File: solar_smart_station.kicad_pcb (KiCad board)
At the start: 6 copper layers, 46 parts, among them J1 CE, J2 CE, J3 Conn_01x03_Pin, J4 JST_VH_B2P_3.96mm, J5 JST_VH_B2P_3.96mm, J6 JST_VH_B3P_3.96mm, U1 BQ25672RQMR, U2 TLV73333PDBV, U3 MSPM0C1104SDSGR

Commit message: First layout
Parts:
- removed J6: JST_VH_B3P_3.96mm, Connector_JST:JST_VH_B3P-VH_1x03_P3.96mm_Vertical
- removed TP2: Thermistor, Connector_PinHeader_2.54mm:PinHeader_1x01_P2.54mm_Vertical
- added C23: 0.1uF, Capacitor_SMD:C_0603_1608Metric, F.Cu at (78.0, 174.5)
- added C24: 0.1uF, Capacitor_SMD:C_0603_1608Metric, F.Cu at (78.0, 171.5)
- added C25: 0.1uF, Capacitor_SMD:C_0603_1608Metric, F.Cu at (78.0, 168.5)
- added C26: 0.1uF, Capacitor_SMD:C_0603_1608Metric, F.Cu at (78.0, 165.5)
- added C27: 0.1uF, Capacitor_SMD:C_0603_1608Metric, F.Cu at (78.0, 162.5)
- added C28: 0.1uF, Capacitor_SMD:C_0603_1608Metric, F.Cu at (78.0, 159.5)
- added C29: 1uF, Capacitor_SMD:C_0603_1608Metric, F.Cu at (72.5, 170.0)
- added C30: 1uF, Capacitor_SMD:C_0603_1608Metric, F.Cu at (68.5, 170.0)
- added C31: 0.1uF, Capacitor_SMD:C_0603_1608Metric, F.Cu at (78.0, 157.0)
- added C32: 0.1uF, Capacitor_SMD:C_0603_1608Metric, F.Cu at (76.5, 155.0)
- added C33: 0.1uF, Capacitor_SMD:C_0603_1608Metric, F.Cu at (79.5, 155.0)
- added D1: LED, LED_SMD:LED_0603_1608Metric, F.Cu at (35.5, 162.0)
- added D2: Schottky_30V_1A, solar_station:DIO_RB02_ROM, F.Cu at (71.5, 157.0)
- added H1: MountingHole_Pad, TestPoint:TestPoint_THTPad_2.5x2.5mm_Drill1.2mm, F.Cu at (84.0, 175.5)
- added H2: MountingHole_Pad, TestPoint:TestPoint_THTPad_2.5x2.5mm_Drill1.2mm, F.Cu at (84.0, 171.5)
- added H3: MountingHole_Pad, TestPoint:TestPoint_THTPad_2.5x2.5mm_Drill1.2mm, F.Cu at (84.0, 167.5)
- added H4: MountingHole_Pad, TestPoint:TestPoint_THTPad_2.5x2.5mm_Drill1.2mm, F.Cu at (84.0, 163.5)
- added H5: MountingHole_Pad, TestPoint:TestPoint_THTPad_2.5x2.5mm_Drill1.2mm, F.Cu at (84.0, 159.5)
- added H6: MountingHole_Pad, TestPoint:TestPoint_THTPad_2.5x2.5mm_Drill1.2mm, F.Cu at (84.0, 155.5)
- added H7: MountingHole_Pad, MountingHole:MountingHole_3.2mm_M3_DIN965_Pad_TopBottom, F.Cu at (34.2, 150.2)
- added H8: MountingHole_Pad, MountingHole:MountingHole_3.2mm_M3_DIN965_Pad_TopBottom, F.Cu at (83.2, 150.0)
- added H9: MountingHole_Pad, MountingHole:MountingHole_3.2mm_M3_DIN965_Pad_TopBottom, F.Cu at (83.2, 181.2)
- added J7: Thermistor_1, Connector_PinHeader_2.54mm:PinHeader_1x02_P2.54mm_Vertical, F.Cu at (51.2, 181.0)
- added J8: Thermistor_2, Connector_PinHeader_2.54mm:PinHeader_1x02_P2.54mm_Vertical, F.Cu at (58.2, 181.0)
- added NT1: NetTie_3, NetTie:NetTie-3_SMD_Pad0.5mm, F.Cu at (47.5, 170.5)
- added NT2: NetTie_2, NetTie:NetTie-2_SMD_Pad0.5mm, F.Cu at (74.5, 179.0)
- added Q1: AO3400A, Package_TO_SOT_SMD:SOT-23, F.Cu at (72.4, 152.0)
- added Q2: AO3400A, Package_TO_SOT_SMD:SOT-23, F.Cu at (68.4, 152.0)
- added R13: 1kR, Resistor_SMD:R_0402_1005Metric, F.Cu at (79.5, 174.5)
- added R14: 1kR, Resistor_SMD:R_0402_1005Metric, F.Cu at (79.5, 171.5)
- added R15: 1kR, Resistor_SMD:R_0402_1005Metric, F.Cu at (79.5, 168.5)
- added R16: 1kR, Resistor_SMD:R_0402_1005Metric, F.Cu at (79.5, 165.5)
- added R17: 1kR, Resistor_SMD:R_0402_1005Metric, F.Cu at (79.5, 162.5)
- added R18: 1kR, Resistor_SMD:R_0402_1005Metric, F.Cu at (79.5, 159.5)
- added R19: 1kR, Resistor_SMD:R_0402_1005Metric, F.Cu at (78.5, 177.0)
- added R20: 100R, Resistor_SMD:R_0402_1005Metric, F.Cu at (79.0, 153.0)
- added R21: 10mR, Resistor_SMD:R_0805_2012Metric, F.Cu at (78.0, 151.0)
- added R22: 100R, Resistor_SMD:R_0402_1005Metric, F.Cu at (77.0, 153.0)
- added R23: 4.7kR, Resistor_SMD:R_0402_1005Metric, F.Cu at (73.5, 157.5)
- added R24: 1MegR, Resistor_SMD:R_0402_1005Metric, F.Cu at (75.0, 152.0)
- added R25: 1MegR, Resistor_SMD:R_0402_1005Metric, F.Cu at (69.5, 156.3)
- added R26: 3.3MegR, Resistor_SMD:R_0402_1005Metric, F.Cu at (65.5, 152.0)
- added R27: 10kR, Resistor_SMD:R_0402_1005Metric, F.Cu at (65.0, 167.0)
- added R28: 100kR, Resistor_SMD:R_0402_1005Metric, F.Cu at (65.0, 163.0)
- added R29: 450kR, Resistor_SMD:R_0402_1005Metric, F.Cu at (65.0, 161.0)
- added R30: 10kR, Resistor_SMD:R_0402_1005Metric, F.Cu at (65.0, 165.0)
- added U4: BQ7791500PWR, solar_station:PW24_TEX, F.Cu at (70.5, 164.5)
- added U5: CSD25402Q3A, Package_SON:VSON-8_3.3x3.3mm_P0.65mm_NexFET, F.Cu at (66.5, 157.0)
- C10, C2, C9: footprint Capacitor_SMD:C_0603_1608Metric -> Capacitor_SMD:C_0402_1005Metric
- J2: value CE -> LDO_EN
- J3: value Conn_01x03_Pin -> Conn_01x05_Pin; footprint Connector_PinSocket_2.54mm:PinSocket_1x03_P2.54mm_Vertical -> Connector_PinHeader_2.54mm:PinHeader_1x05_P2.54mm_Vertical
- U3: footprint Package_TO_SOT_SMD:TSOT-23-8 -> solar_station:TSOT-23-8-shrink
- moved J4 51.7 mm to (32.7, 179.9)
- moved C18 33.6 mm to (58.0, 158.5), turned to -90 degrees
- moved J3 32.5 mm to (75.1, 181.0), turned to -90 degrees
- moved C21 31.8 mm to (44.5, 170.5), turned to 180 degrees
- moved C22 31.2 mm to (44.5, 172.0), turned to 180 degrees
- moved R12 29.5 mm to (43.5, 175.5), turned to 90 degrees
- moved R9 28.8 mm to (47.0, 172.0), turned to 180 degrees
- moved J5 28.3 mm to (61.3, 151.3), turned to 180 degrees
- moved R11 28.3 mm to (48.5, 176.5), turned to 90 degrees
- moved R10 28.3 mm to (48.5, 174.5), turned to -90 degrees
- moved C16 27.5 mm to (55.5, 158.5), turned to -90 degrees
- moved C14 26.7 mm to (59.2, 163.5), turned to 90 degrees
- moved U3 26.3 mm to (46.0, 175.5), turned to -90 degrees
- moved C11 24.7 mm to (56.8, 163.5), turned to 90 degrees
- moved L1 22.7 mm to (48.5, 152.0)
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- renumbered C22 to C20, C20 to C21, C21 to C22
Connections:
- net +12V renamed +21V
- net Net-(J1-Pin_1) renamed CE_N
- net Net-(J2-Pin_2) renamed LDO_IN
- net Net-(J3-Pin_2) renamed SWDIO
- net Net-(J3-Pin_3) renamed SWCLK
- J3 pad 1: /Project Architecture/MCU/SCL -> VCC
- R10 pad 2: /Project Architecture/MCU/INT_N -> INT_N
- R12 pad 1: /Project Architecture/MCU/SDA -> SDA
- R9 pad 2: /Project Architecture/MCU/SCL -> /Project Architecture/MCU/SCL/RST
- U1 pad 14: /Project Architecture/SolarCharger/SCL -> SCL
- U1 pad 15: /Project Architecture/SolarCharger/SDA -> SDA
- U1 pad 21: /Project Architecture/SolarCharger/INT_N -> INT_N
- U3 pad 1: /Project Architecture/MCU/INT_N -> INT_N
- U3 pad 2: /Project Architecture/MCU/SCL -> /Project Architecture/MCU/SCL/RST
- U3 pad 5: /Project Architecture/MCU/SDA -> SDA
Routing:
- net +3V3: track 0.00 -> 51.2 mm, vias 0 -> 4
- net GND: track 0.00 -> 37.4 mm, vias 0 -> 16
- net REGN: track 0.00 -> 34.1 mm, vias 0 -> 3
- net +21V: track 0.00 -> 32.3 mm
- net SWDIO: track 0.00 -> 31.0 mm, vias 0 -> 1
- net SWCLK: track 0.00 -> 27.3 mm, vias 0 -> 1
- net BATTERY_PACK: track 0.00 -> 26.1 mm, vias 0 -> 13
- net RST: track 0.00 -> 23.3 mm, vias 0 -> 1
- net THERMISTOR_2: track 0.00 -> 22.2 mm
- net Net-(U4-VDD): track 0.00 -> 21.9 mm
- net SYSTEM_LOAD: track 0.00 -> 21.6 mm
- net CE_N: track 0.00 -> 18.5 mm, vias 0 -> 1
- net THERMISTOR: track 0.00 -> 18.3 mm
- net INT_N: track 0.00 -> 17.2 mm, vias 0 -> 2
- net Net-(U1-SW2): track 0.00 -> 16.7 mm, vias 0 -> 7
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- added copper zone on F.Cu, net -BATT
- added copper zone on In1.Cu, net -BATT
- added copper zone on B.Cu, net BATTERY_PACK
- added copper zone on F.Cu, net BATTERY_PACK
- added copper zone on F.Cu, net GND
- added copper zone on In1.Cu, net GND
- added copper zone on F.Cu, net Net-(U1-SW1)
- added copper zone on F.Cu, net Net-(U1-SW2)
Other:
- board outline added: 57.8 x 39.5 mm
- copper layers 6 -> 4

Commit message: Finish layout
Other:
- board text added: "BAT+"
- board text added: "BAT-"
- board text added: "CE"
- board text added: "GND"
- board text added: "IN+"
- board text added: "LOAD"
- board text added: "Max 21V"
- board text added: "RST"
- board text added: "SWCLK"
- board text added: "SWD PRG"
- board text added: "SWDIO"
- board text added: "Ther1"
- board text added: "Ther2"
- board text added: "VC1"
- board text added: "VC2"
- board text added: "VC3"
- board text added: "VC4"
- board text added: "VCC"
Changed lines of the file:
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@@
 	)
 	(property "ASSEMBLY_NOTES" "")
-	(property "BOARD_NAME" "Board Name")
-	(property "COMPANY" "Company Name")
-	(property "DESIGNER" "Author")
+	(property "BOARD_NAME" "Balanced Solar Charger")
+	(property "COMPANY" "Electronic-Handyman")
+	(property "DESIGNER" "Nhan Duy Truong")
 	(property "FABRICATION_NOTES" "")
 	(property "GIT_HASH_PCB" "23fc206")
 	(property "GIT_HASH_SCH" "8e341b7")
-	(property "GIT_URL" "https://github.com/nguyen-v/KDT_Hierarchical_KiBot")
-	(property "PROJECT_NAME" "KiBot Project")
+	(property "GIT_URL" "https://github.com/truongduynhan/solar_smart_station.git")
+	(property "PROJECT_NAME" "LiPo Battery Charger with CI/CD using KiBot")
 	(property "RELEASE_BODY_1.0.0" "")
 	(property "RELEASE_BODY_1.0.1" "")
@@
 		(tags "Through hole pin header THT 1x05 2.54mm single row")
 		(property "Reference" "J3"
-			(at -2.5 6.33 180)
+			(at 0 -2.67 180)
 			(layer "F.SilkS")
 			(effects
@@
 		)
 		(embedded_fonts no)
-		(model "${KICAD9_3DMODEL_DIR}/Inductor_SMD.3dshapes/L_Bourns_SRP7028A_7.3x6.6mm.step"
+		(model "${KIPRJMOD}/libraries/3D/IHLP2525CZ.step"
 			(offset
-				(xyz 0 0 0)
+				(xyz -1.5 5.325 -2.4)
 			)
 			(scale
@@
 			)
 			(rotate
-				(xyz 0 0 0)
+				(xyz -90 -0 -0)
 			)
 		)
@@
 		(tags "RSX101VYM30FHTR ")
 		(property "Reference" "D2"
-			(at -2.677507 -0.09567 0)
+			(at -2 -1.75 0)
 			(unlocked yes)
 			(layer "F.SilkS")
@@
 		(layer "User.9")
 	)
+	(gr_text "SWDIO"
+		(at 73.25 179.25 90)
+		(layer "F.SilkS")
+		(effects
+			(font
+				(size 1.2 1.2)
+				(thickness 0.15)
+			)
+			(justify left bottom)
+		)
+	)
+	(gr_text "SWD PRG"
+		(at 64.75 184.75 0)
+		(layer "F.SilkS")
+		(effects
+			(font
+				(size 1.6 1.6)
+				(thickness 0.15)
+			)
+			(justify left bottom)
+		)
+	)
+	(gr_text "Ther1"
+		(at 49.5 184.75 0)
+		(layer "F.SilkS")
+		(effects
+			(font
+				(size 1.6 1.6)
+				(thickness 0.15)
+			)
+			(justify left bottom)
+		)
+	)
+	(gr_text "VCC"
+		(at 76 179 90)
+		(layer "F.SilkS")
+		(effects
+			(font
+				(size 1.2 1.2)
+				(thickness 0.15)
+			)
+			(justify left bottom)
+		)
+	)
+	(gr_text "RST"
+		(at 68.25 179.25 90)
+		(layer "F.SilkS")
+		(effects
+			(font
+				(size 1.2 1.2)
+				(thickness 0.15)
+			)
+			(justify left bottom)
+		)
+	)
+	(gr_text "GND"
+		(at 65.75 179.25 90)
+		(layer "F.SilkS")
+		(effects
+			(font
+				(size 1.2 1.2)
+				(thickness 0.15)
+			)
+			(justify left bottom)
+		)
+	)
+	(gr_text "Ther2"
+		(at 56.25 184.75 0)
+		(layer "F.SilkS")
+		(effects
+			(font
+				(size 1.6 1.6)
+				(thickness 0.15)
+			)
+			(justify left bottom)
+		)
+	)
+	(gr_text "SWCLK"
+		(at 70.75 179.25 90)
+		(layer "F.SilkS")
+		(effects
+			(font
+				(size 1.2 1.2)
+				(thickness 0.15)
+			)
+			(justify left bottom)
+		)
+	)
+	(gr_text "CE"
+		(at 44 184.75 0)
+		(layer "F.SilkS")
+		(effects
+			(font
+				(size 1.6 1.6)
+				(thickness 0.15)
+			)
+			(justify left bottom)
+		)
+	)
+	(gr_text "BAT+"
+		(at 81.5 177 0)
+		(layer "B.SilkS")
+		(effects
+			(font
+				(size 2.5 2.5)
+				(thickness 0.5)
+				(bold yes)
+			)
+			(justify left bottom mirror)
+		)
+	)
+	(gr_text "VC4"
+		(at 81.5 173 0)
+		(layer "B.SilkS")
+		(effects
+			(font
+				(size 2.5 2.5)
+				(thickness 0.5)
+				(bold yes)
+			)
+			(justify left bottom mirror)
+		)
+	)
+	(gr_text "Max 21V"
+		(at 35 177.75 270)
+		(layer "B.SilkS")
+		(effects
+			(font
+				(size 2 2)
+				(thickness 0.3125)
+			)
+			(justify left bottom mirror)
+		)
+	)
+	(gr_text "LOAD"
+		(at 62.75 153.25 90)
+		(layer "B.SilkS")
+		(effects
+			(font
+				(size 2.5 2.5)
+				(thickness 0.5)
+				(bold yes)
+			)
+			(justify left bottom mirror)
+		)
+	)
+	(gr_text "IN+"
+		(at 31 178 270)
+		(layer "B.SilkS")
+		(effects
+			(font
+				(size 2.5 2.5)
+				(thickness 0.5)
+				(bold yes)
+			)
+			(justify left bottom mirror)
+		)
+	)
+	(gr_text "VC3"
+		(at 81.5 169 0)
+		(layer "B.SilkS")
+		(effects
+			(font
+				(size 2.5 2.5)
+				(thickness 0.5)
+				(bold yes)
+			)
+			(justify left bottom mirror)
+		)
+	)
+	(gr_text "VC2"
+		(at 81.5 164.75 0)
+		(layer "B.SilkS")
+		(effects
+			(font
+				(size 2.5 2.5)
+				(thickness 0.5)
+				(bold yes)
+			)
+			(justify left bottom mirror)
+		)
+	)
+	(gr_text "VC1"
+		(at 81.5 161 0)
+		(layer "B.SilkS")
+		(effects
+			(font
+				(size 2.5 2.5)
+				(thickness 0.5)
+				(bold yes)
+			)
+			(justify left bottom mirror)
+		)
+	)
+	(gr_text "BAT-"
+		(at 81.5 156.75 0)
+		(layer "B.SilkS")
+		(effects
+			(font
+				(size 2.5 2.5)
+				(thickness 0.5)
+				(bold yes)
+			)
+			(justify left bottom mirror)
+		)
+	)
 	(gr_text "Top View"
 		(at 83.5 40 0)
@@
 	)
 	(zone
-		(net 2)
-		(net_name "GND")
+		(net 30)
+		(net_name "-BATT")
 		(layer "In1.Cu")
-		(name "L1_GND")
 		(hatch edge 0.5)
-		(connect_pads thru_hole_only
-			(clearance 0.2)
+		(priority 2)
+		(connect_pads yes
+			(clearance 0)
 		)
 		(min_thickness 0.25)
@@
 		(polygon
 			(pts
-				(xy 30.75 146.75) (xy 70 146.5) (xy 70 184.75) (xy 30.75 185)
+				(xy 70 146.5) (xy 86.75 146.5) (xy 86.75 184.75) (xy 64 184.75) (xy 64 154.75) (xy 70 154.75)
 			)
 		)
 	)
 	(zone
-		(net 30)
-		(net_name "-BATT")
+		(net 2)
+		(net_name "GND")
 		(layer "In1.Cu")
+		(name "L1_GND")
 		(hatch edge 0.5)
-		(priority 2)
-		(connect_pads yes
-			(clearance 0)
+		(connect_pads thru_hole_only
+			(clearance 0.2)
 		)
 		(min_thickness 0.25)
@@
 		(polygon
 			(pts
-				(xy 70 146.5) (xy 86.75 146.5) (xy 86.75 184.75) (xy 64 184.75) (xy 64 154.75) (xy 70 154.75)
+				(xy 30.75 146.75) (xy 70 146.5) (xy 70 184.75) (xy 30.75 185)
 			)
 		)

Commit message: Fix ERC
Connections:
- net REGN renamed REGN_5V
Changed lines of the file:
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@@
 	(net 19 "Net-(D1-K)")
 	(net 20 "+21V")
-	(net 21 "REGN")
+	(net 21 "REGN_5V")
 	(net 22 "Net-(U3-PA24{slash}A3)")
 	(net 23 "/Project Architecture/SolarCharger/QON")
@@
 			(layers "F.Cu" "F.Mask" "F.Paste")
 			(roundrect_rratio 0.25)
-			(net 21 "REGN")
+			(net 21 "REGN_5V")
 			(pintype "passive")
 		)
@@
 			(layers "*.Cu" "*.Mask")
 			(remove_unused_layers no)
-			(net 21 "REGN")
+			(net 21 "REGN_5V")
 			(pinfunction "Pin_1")
 			(pintype "passive")
@@
 			(layers "F.Cu" "F.Mask" "F.Paste")
 			(roundrect_rratio 0.25)
-			(net 21 "REGN")
+			(net 21 "REGN_5V")
 			(pintype "passive")
 		)
@@
 			(layers "F.Cu" "F.Mask" "F.Paste")
 			(roundrect_rratio 0.25)
-			(net 21 "REGN")
+			(net 21 "REGN_5V")
 			(pintype "passive")
 		)
@@
 			(layers "F.Cu" "F.Mask" "F.Paste")
 			(roundrect_rratio 0.25)
-			(net 21 "REGN")
+			(net 21 "REGN_5V")
 			(pintype "passive")
 		)
@@
 			(size 0.599999 0.2)
 			(layers "F.Cu" "F.Mask" "F.Paste")
-			(net 21 "REGN")
+			(net 21 "REGN_5V")
 			(pinfunction "REGN")
 			(pintype "unspecified")

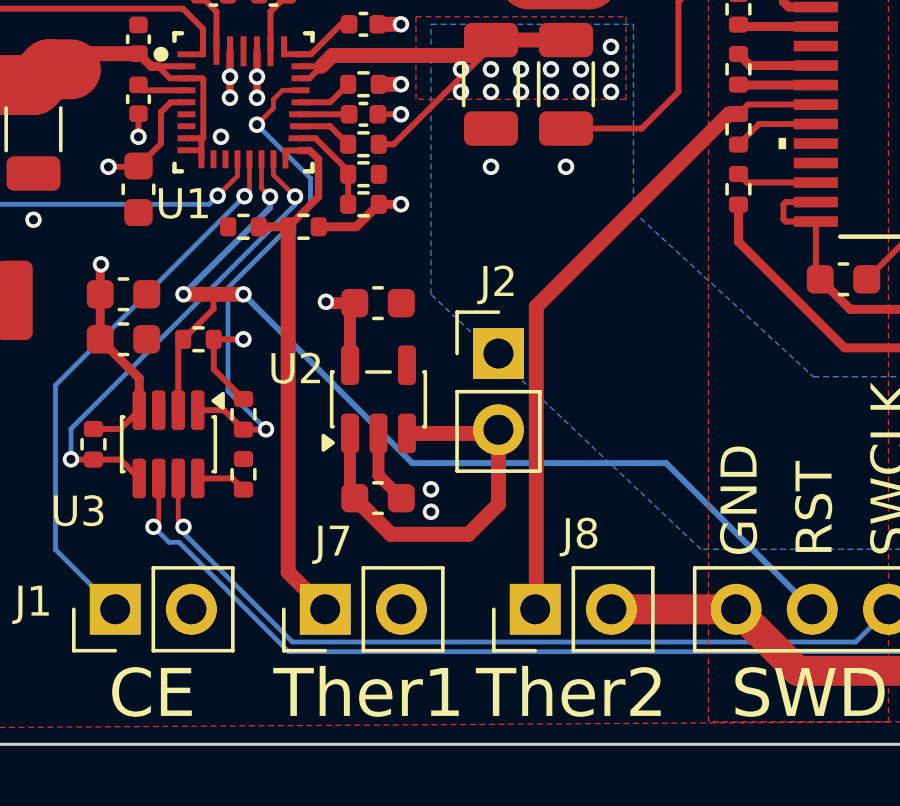
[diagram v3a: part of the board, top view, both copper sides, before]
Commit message: All connectors are deemed the same in BOM. Re-push.
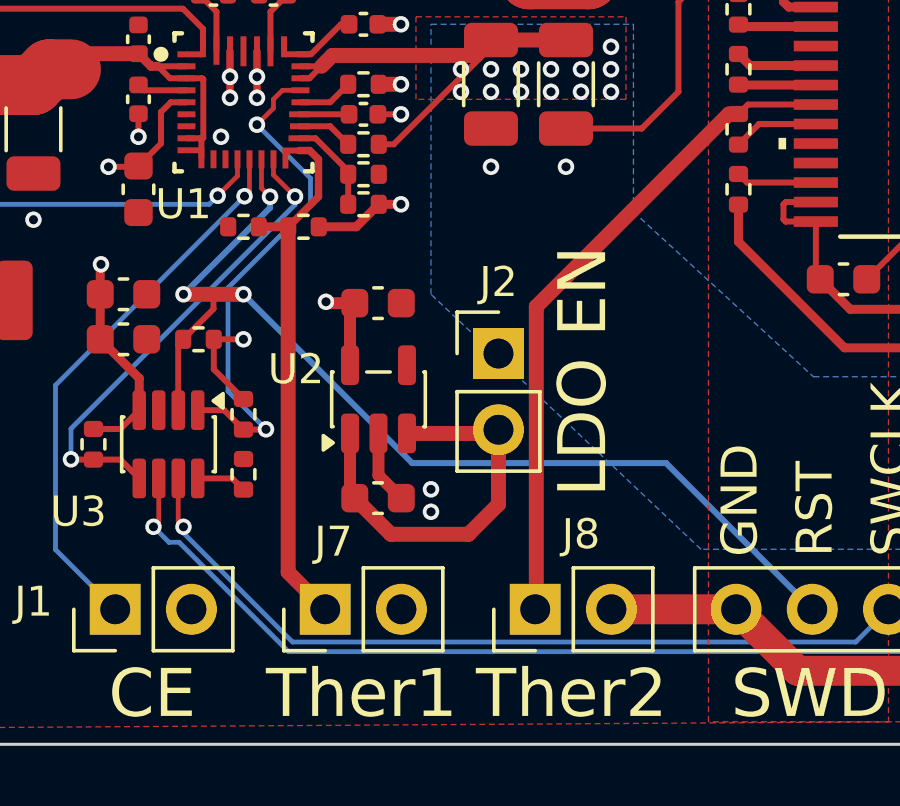
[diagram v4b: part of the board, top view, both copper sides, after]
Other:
- board text added: "LDO EN"
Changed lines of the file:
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@@
 	)
 	(gr_text "Ther1"
-		(at 49.5 184.75 0)
+		(at 49.25 184.75 0)
 		(layer "F.SilkS")
 		(effects
@@
 				(thickness 0.15)
 			)
+			(justify left bottom)
+		)
+	)
+	(gr_text "LDO EN"
+		(at 60.75 177.25 90)
+		(layer "F.SilkS")
+		(effects
+			(font
+				(size 1.6 1.6)
+				(thickness 0.15)
+			)

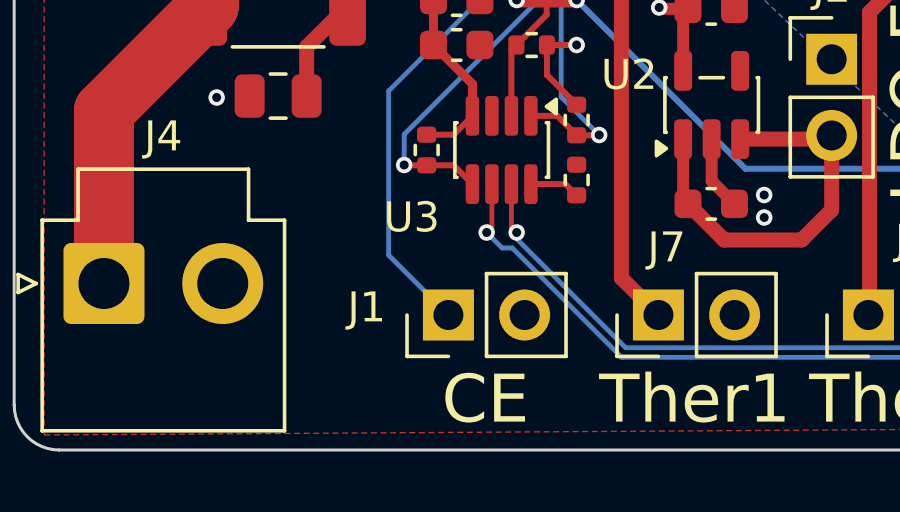
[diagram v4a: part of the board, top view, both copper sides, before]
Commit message: Replace jumper to force BOM updated
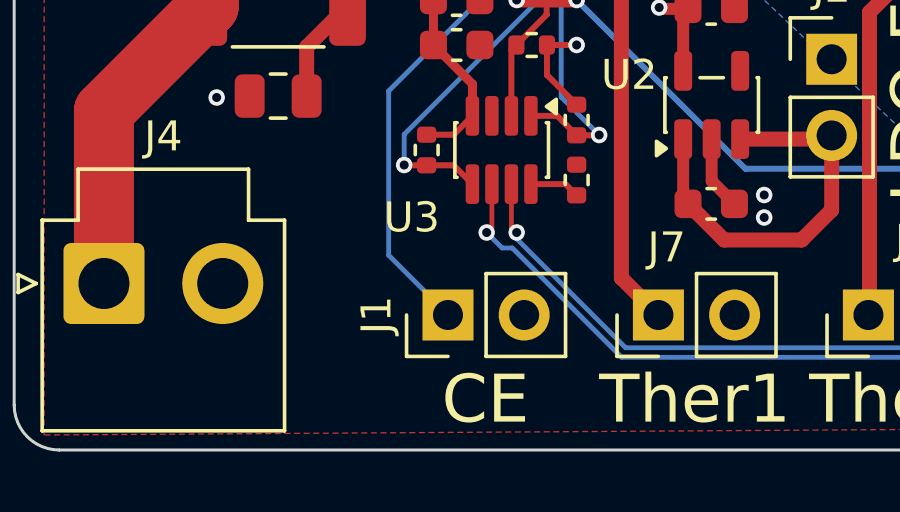
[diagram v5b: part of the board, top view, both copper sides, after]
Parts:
- J1: value CE -> Conn_01x02_Pin

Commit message: Finish checking - Ready for 1st release
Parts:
- renumbered J7 to J4, J8 to J5, J4 to JST1, J5 to JST2
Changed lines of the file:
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@@
 		(descr "Through hole straight pin header, 1x02, 2.54mm pitch, single row")
 		(tags "Through hole pin header THT 1x02 2.54mm single row")
-		(property "Reference" "J8"
+		(property "Reference" "J5"
 			(at 2.5 1.525 180)
 			(layer "F.SilkS")
@@
 		(descr "Through hole straight pin header, 1x02, 2.54mm pitch, single row")
 		(tags "Through hole pin header THT 1x02 2.54mm single row")
-		(property "Reference" "J7"
+		(property "Reference" "J4"
 			(at 2.25 0.275 0)
 			(layer "F.SilkS")
@@
 		(descr "JST VH series connector, B2P-VH (http://www.jst-mfg.com/product/pdf/eng/eVH.pdf), generated with kicad-footprint-generator")
 		(tags "connector JST VH vertical")
-		(property "Reference" "J5"
+		(property "Reference" "JST2"
 			(at 7.5075 3.3 0)
 			(layer "F.SilkS")
@@
 		(descr "JST VH series connector, B2P-VH (http://www.jst-mfg.com/product/pdf/eng/eVH.pdf), generated with kicad-footprint-generator")
 		(tags "connector JST VH vertical")
-		(property "Reference" "J4"
+		(property "Reference" "JST1"
 			(at 1.98 -4.9 0)
 			(layer "F.SilkS")

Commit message: Ready for 1st release
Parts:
- moved U5 1.21 mm to (65.5, 157.7)
- moved C23 1.00 mm to (77.0, 174.5)
- moved C24 1.00 mm to (77.0, 171.5)
- moved C25 1.00 mm to (77.0, 168.5)
- moved C26 1.00 mm to (77.0, 165.5)
- moved C27 1.00 mm to (77.0, 162.5)
- moved C28 1.00 mm to (77.0, 159.5)
- moved C29 1.00 mm to (71.5, 170.0)
- moved C30 1.00 mm to (67.5, 170.0)
- moved C31 1.00 mm to (77.0, 157.0)
- moved C32 1.00 mm to (75.5, 155.0)
- moved C33 1.00 mm to (78.5, 155.0)
- moved D2 1.00 mm to (70.5, 157.0)
- moved H1 1.00 mm to (83.0, 175.5)
- moved H2 1.00 mm to (83.0, 171.5)
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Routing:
- net GND: track 37.4 -> 36.4 mm
- net Net-(U4-CHG): track 4.52 -> 3.83 mm

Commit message: Ready for 1st release
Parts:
- JST1, JST2: value JST_VH_B2P_3.96mm -> Conn_01x02_Socket
